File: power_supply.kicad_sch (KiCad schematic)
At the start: 40 parts, among them J1 USB_C_Receptacle_USB2.0_16P, J2 B2B-XH-A, J3 USB_C_Receptacle_USB2.0_16P, SW1 SW_SPDT

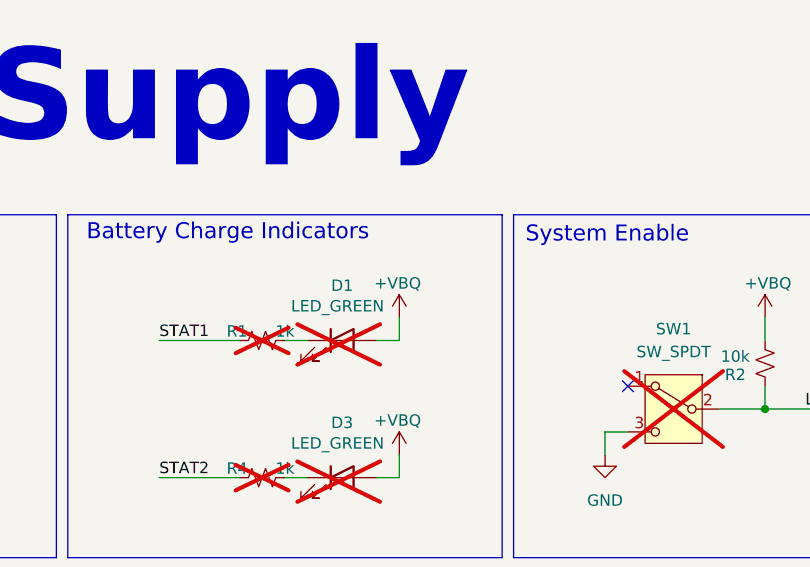
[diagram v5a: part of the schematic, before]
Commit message: feat: places power circuitry with microcontroller
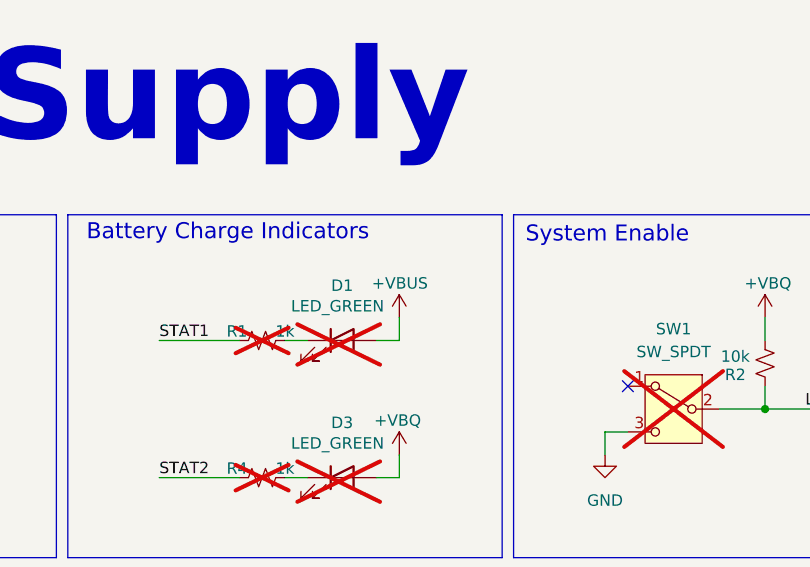
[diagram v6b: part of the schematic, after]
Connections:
- net +VBQ: no longer D1.2 (A)
- net +VBUS: now also D1.2 (A)
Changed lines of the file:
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@@
-	)
-	(symbol
-		(lib_id "power:VBUS")
-		(at 199.39 46.99 0)
-		(unit 1)
-		(exclude_from_sim no)
-		(in_bom yes)
-		(on_board yes)
-		(dnp no)
-		(property "Reference" "#PWR03"
-			(at 199.39 50.8 0)
-			(effects
-				(font
-					(size 1.27 1.27)
-				)
-				(hide yes)
-			)
-		)
-		(property "Value" "+VBQ"
-			(at 196.596 43.18 0)
-			(effects
-				(font
-					(size 1.27 1.27)
-				)
-				(justify left)
-			)
-		)
-		(property "Footprint" ""
-			(at 199.39 46.99 0)
-			(effects
-				(font
-					(size 1.27 1.27)
-				)
-				(hide yes)
-			)
-		)
-		(property "Datasheet" ""
-			(at 199.39 46.99 0)
-			(effects
-				(font
-					(size 1.27 1.27)
-				)
-				(hide yes)
-			)
-		)
-		(property "Description" "Power symbol creates a global label with name \"VBUS\""
-			(at 199.39 46.99 0)
-			(effects
-				(font
-					(size 1.27 1.27)
-				)
-				(hide yes)
-			)
-		)
-		(pin "1"
-		)
-		(instances
-			(project "zbook"
-				(path "/b90666d0-8852-4bb1-832d-f9d855027372/d670a894-5140-4373-b43b-8923af8a146b"
-					(reference "#PWR03")
-					(unit 1)
-				)
-			)
-		)
 	)
 	(symbol
@@
 					(unit 1)
 				)
+			)
+		)
+	)
+	(symbol
+		(lib_id "power:VBUS")
+		(at 199.39 46.99 0)
+		(unit 1)
+		(exclude_from_sim no)
+		(in_bom yes)
+		(on_board yes)
+		(dnp no)
+		(property "Reference" "#PWR03"
+			(at 199.39 50.8 0)
+			(effects
+				(font
+					(size 1.27 1.27)
+				)
+				(hide yes)
+			)
+		)
+		(property "Value" "+VBUS"
+			(at 196.342 43.18 0)
+			(effects
+				(font
+					(size 1.27 1.27)
+				)
+				(justify left)
+			)
+		)
+		(property "Footprint" ""
+			(at 199.39 46.99 0)
+			(effects
+				(font
+					(size 1.27 1.27)
+				)
+				(hide yes)
+			)
+		)
+		(property "Datasheet" ""
+			(at 199.39 46.99 0)
+			(effects
+				(font
+					(size 1.27 1.27)
+				)
+				(hide yes)
+			)
+		)
+		(property "Description" "Power symbol creates a global label with name \"VBUS\""
+			(at 199.39 46.99 0)
+			(effects
+				(font
+					(size 1.27 1.27)
+				)
+				(hide yes)
+			)
+		)
+		(pin "1"
+		)
+		(instances
+			(project "zbook"
+				(path "/b90666d0-8852-4bb1-832d-f9d855027372/d670a894-5140-4373-b43b-8923af8a146b"
+					(reference "#PWR03")
+					(unit 1)
+				)

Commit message: feat: starts routing
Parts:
- D5, R12: now not fitted
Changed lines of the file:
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@@
 		(in_bom yes)
 		(on_board yes)
-		(dnp no)
+		(dnp yes)
 		(property "Reference" "R12"
 			(at 203.708 106.934 90)
@@
 		(in_bom yes)
 		(on_board yes)
-		(dnp no)
+		(dnp yes)
 		(property "Reference" "D5"
 			(at 198.12 114.046 0)

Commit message: wip: adds more routing
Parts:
- removed C3, C4, C5: 10u, Capacitor_SMD:C_0805_2012Metric, symbol Device:C_Small
- removed D1, D3, D5: LED_GREEN, LED_SMD:LED_0603_1608Metric, symbol Device:LED
- removed J2: B2B-XH-A, B2B-XH-A:JST_B2B-XH-A, symbol B2B-XH-A:B2B-XH-A
- removed R1, R12, R4, R9: 1k, Resistor_SMD:R_0402_1005Metric, symbol Device:R_Small_US
- removed R10, R2: 10k, Resistor_SMD:R_0402_1005Metric, symbol Device:R_Small_US
- removed R6, R7: 0R, Resistor_SMD:R_1206_3216Metric, symbol Device:R_Small_US
- removed R8: 20k, Resistor_SMD:R_0402_1005Metric, symbol Device:R_Small_US
- removed SW1: SW_SPDT, power_supply:SW_SLW-121456-3A-N-D, symbol Switch:SW_SPDT
- removed TP4: TestPoint_Small, TestPoint:TestPoint_Pad_D1.0mm, symbol Connector:TestPoint_Small
- removed U2: ~, power_supply:WSON10_DLH_TEX, symbol Power_PMIC_TexasInstruments_BQ25185:BQ25185DLHR
- renumbered D2 to D1, D7 to D2, D4 to D3, D6 to D4, J3 to J2, R3 to R1, R5 to R2, R14 to R3, R11 to R4, R13 to R5, R15 to R6, TP3 to TP1, TP1 to TP2, TP2 to TP3, TP5 to TP4, TP6 to TP5, TP7 to TP6
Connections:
- net +VBQ is gone; now on net +VBUS: C1.1, TP2.1, U1.1 (IN)
- net LDO_EN is gone; now on net +VBUS: U1.3 (EN)
- no-connect marks 8 -> 7
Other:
- note removed: "BQ Bypass"
- note removed: "Battery Charge Indicators"
- note removed: "Battery Header"
- note removed: "Battery Management"
- note removed: "System Enable"
- moved on the sheet: C1, C2, D1, D2, D3, D4, J1, J2, R1, R2, R3, R4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
